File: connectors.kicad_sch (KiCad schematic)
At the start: 4 parts, among them J1 Conn_01x04_Pin, J2 Conn_01x04_Pin, J3 Conn_01x08_Pin, J4 Conn_02x03_Odd_Even

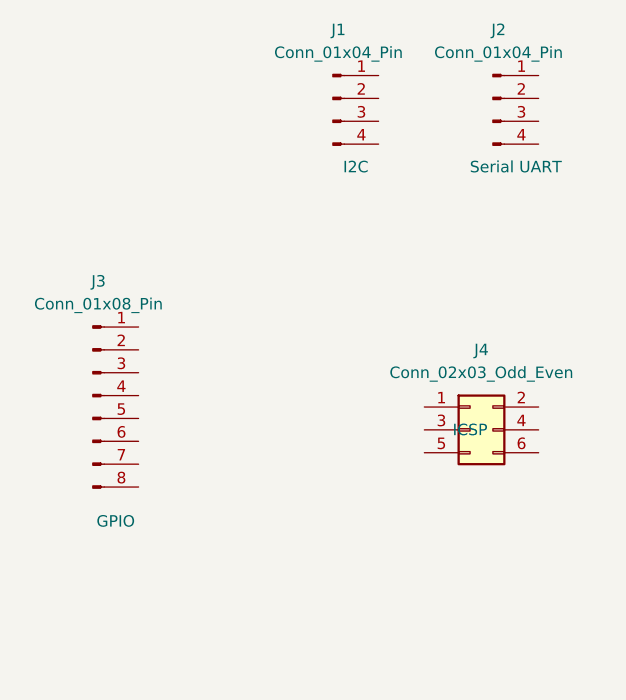
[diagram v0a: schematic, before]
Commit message: changed location of components
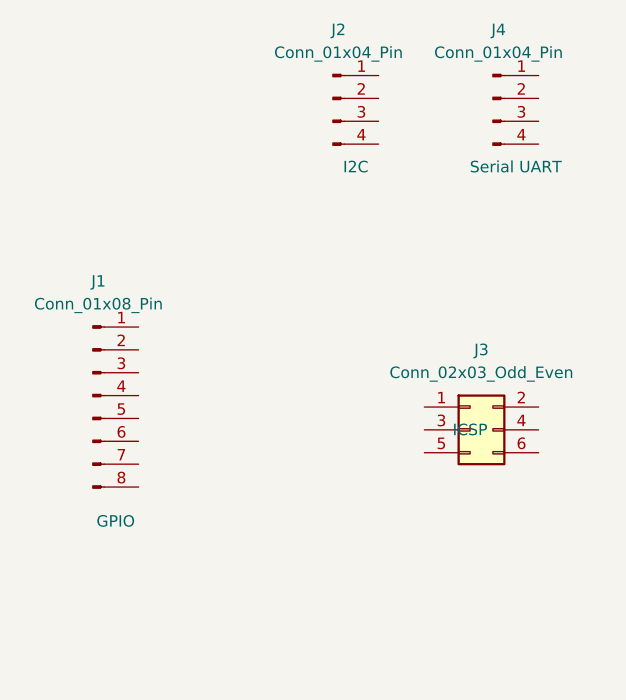
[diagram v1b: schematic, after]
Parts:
- renumbered J3 to J1, J1 to J2, J4 to J3, J2 to J4
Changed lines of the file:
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@@
 		(dnp no)
 		(fields_autoplaced yes)
-		(property "Reference" "J4"
+		(property "Reference" "J3"
 			(at 142.24 121.92 0)
 			(effects
@@
 			(project ""
 				(path "/f5eacbf3-5133-41a8-b529-b36a541e7d42/3a63fbca-d63c-4992-8461-2559cf5d4fe8"
-					(reference "J4")
+					(reference "J3")
 					(unit 1)
 				)
@@
 		(on_board yes)
 		(dnp no)
-		(property "Reference" "J1"
+		(property "Reference" "J2"
 			(at 126.365 86.36 0)
 			(effects
@@
 			(project ""
 				(path "/f5eacbf3-5133-41a8-b529-b36a541e7d42/3a63fbca-d63c-4992-8461-2559cf5d4fe8"
-					(reference "J1")
+					(reference "J2")
 					(unit 1)
 				)
@@
 		(on_board yes)
 		(dnp no)
-		(property "Reference" "J3"
+		(property "Reference" "J1"
 			(at 99.695 114.3 0)
 			(effects
@@
 			(project ""
 				(path "/f5eacbf3-5133-41a8-b529-b36a541e7d42/3a63fbca-d63c-4992-8461-2559cf5d4fe8"
-					(reference "J3")
+					(reference "J1")
 					(unit 1)
 				)
@@
 		(on_board yes)
 		(dnp no)
-		(property "Reference" "J2"
+		(property "Reference" "J4"
 			(at 144.145 86.36 0)
 			(effects
@@
 			(project "MCU Datalogger"
 				(path "/f5eacbf3-5133-41a8-b529-b36a541e7d42/3a63fbca-d63c-4992-8461-2559cf5d4fe8"
-					(reference "J2")
+					(reference "J4")
 					(unit 1)
 				)

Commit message: Added 3rd party footprints
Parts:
- removed J1: Conn_01x08_Pin, symbol Connector:Conn_01x08_Pin
- added J1: Conn_01x09_Pin, Connector_PinHeader_2.54mm:PinHeader_1x09_P2.54mm_Vertical, symbol Connector:Conn_01x09_Pin
- J2, J4: footprint (none) -> Connector_PinHeader_2.54mm:PinHeader_1x04_P2.54mm_Vertical
- J3: footprint (none) -> Connector_PinHeader_2.54mm:PinHeader_2x03_P2.54mm_Vertical
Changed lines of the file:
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@@
 			)
 		)
-		(property "Footprint" ""
+		(property "Footprint" "Connector_PinHeader_2.54mm:PinHeader_2x03_P2.54mm_Vertical"
 			(at 140.97 130.81 0)
 			(effects
@@
 			)
 		)
-		(property "Footprint" ""
+		(property "Footprint" "Connector_PinHeader_2.54mm:PinHeader_1x04_P2.54mm_Vertical"
 			(at 125.73 93.98 0)
 			(effects
@@
 	)
 	(symbol
-		(lib_id "Connector:Conn_01x08_Pin")
-		(at 99.06 127 0)
+		(lib_id "Connector:Conn_01x09_Pin")
+		(at 110.49 144.78 0)
 		(unit 1)
 		(exclude_from_sim no)
@@
 		(dnp no)
 		(property "Reference" "J1"
-			(at 99.695 114.3 0)
-			(effects
-				(font
-					(size 1.27 1.27)
-				)
-			)
-		)
-		(property "Value" "Conn_01x08_Pin"
-			(at 99.695 116.84 0)
-			(effects
-				(font
-					(size 1.27 1.27)
-				)
-			)
-		)
-		(property "Footprint" ""
-			(at 99.06 127 0)
+			(at 111.125 129.54 0)
+			(effects
+				(font
+					(size 1.27 1.27)
+				)
+			)
+		)
+		(property "Value" "Conn_01x09_Pin"
+			(at 111.125 132.08 0)
+			(effects
+				(font
+					(size 1.27 1.27)
+				)
+			)
+		)
+		(property "Footprint" "Connector_PinHeader_2.54mm:PinHeader_1x09_P2.54mm_Vertical"
+			(at 110.49 144.78 0)
 			(effects
 				(font
@@
 		)
 		(property "Datasheet" "~"
-			(at 99.06 127 0)
-			(effects
-				(font
-					(size 1.27 1.27)
-				)
-				(hide yes)
-			)
-		)
-		(property "Description" "Generic connector, single row, 01x08, script generated"
-			(at 99.06 127 0)
+			(at 110.49 144.78 0)
+			(effects
+				(font
+					(size 1.27 1.27)
+				)
+				(hide yes)
+			)
+		)
+		(property "Description" "Generic connector, single row, 01x09, script generated"
+			(at 110.49 144.78 0)
 			(effects
 				(font
@@
 		)
 		(property "Purpose" "GPIO"
-			(at 101.6 140.97 0)
-			(effects
-				(font
-					(size 1.27 1.27)
-				)
-			)
+			(at 113.03 157.48 0)
+			(effects
+				(font
+					(size 1.27 1.27)
+				)
+			)
+		)
+		(pin "3"
+		)
+		(pin "4"
 		)
 		(pin "5"
 		)
-		(pin "3"
-		)
-		(pin "4"
+		(pin "9"
+		)
+		(pin "8"
+		)
+		(pin "2"
+		)
+		(pin "6"
 		)
 		(pin "7"
 		)
-		(pin "2"
-		)
 		(pin "1"
-		)
-		(pin "6"
-		)
-		(pin "8"
 		)
 		(instances
@@
 			)
 		)
-		(property "Footprint" ""
+		(property "Footprint" "Connector_PinHeader_2.54mm:PinHeader_1x04_P2.54mm_Vertical"
 			(at 143.51 93.98 0)
 			(effects

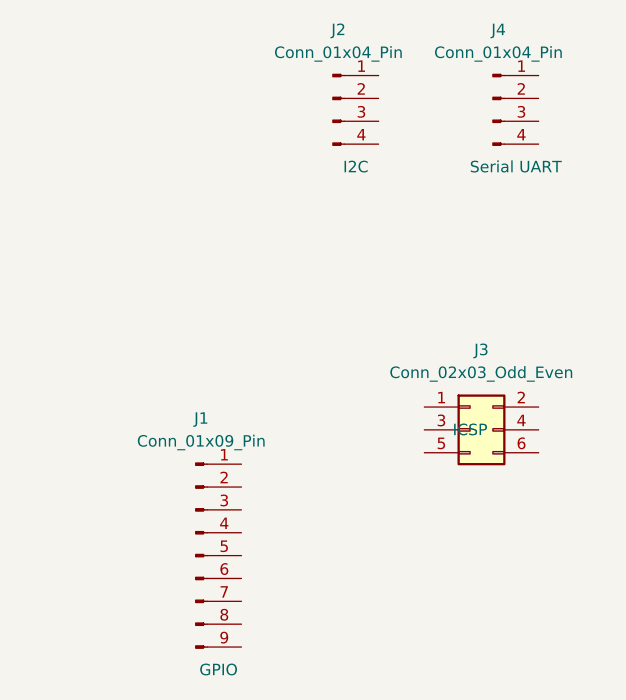
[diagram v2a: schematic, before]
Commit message: Wired connectors sheet
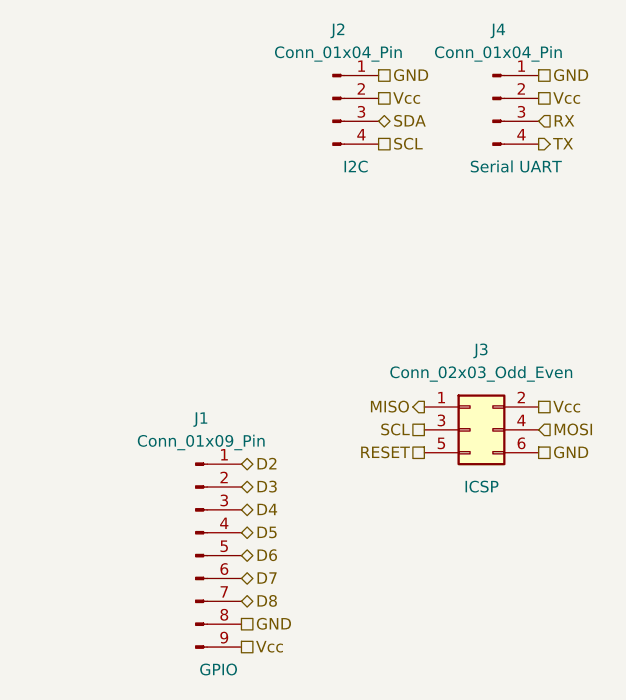
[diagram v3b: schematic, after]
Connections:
- net MISO: now reaches J3.1 (Pin_1)
- net Vcc: now reaches J3.2 (Pin_2)
- net Vcc: now also J1.9 (Pin_9), J2.2 (Pin_2), J4.2 (Pin_2)
- net SCL: now reaches J3.3 (Pin_3)
- net SCL: now also J2.4 (Pin_4)
- net MOSI: now reaches J3.4 (Pin_4)
- net RESET: now reaches J3.5 (Pin_5)
- net GND: now reaches J3.6 (Pin_6)
- net GND: now also J1.8 (Pin_8), J2.1 (Pin_1), J4.1 (Pin_1)
- net SDA: now reaches J2.3 (Pin_3)
- net D2: now reaches J1.1 (Pin_1)
- net D3: now reaches J1.2 (Pin_2)
- net D4: now reaches J1.3 (Pin_3)
- net D5: now reaches J1.4 (Pin_4)
- net D6: now reaches J1.5 (Pin_5)
- net D7: now reaches J1.6 (Pin_6)
- net D8: now reaches J1.7 (Pin_7)
- net RX: now reaches J4.3 (Pin_3)
- net TX: now reaches J4.4 (Pin_4)

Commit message: Fixed errors in the schematic
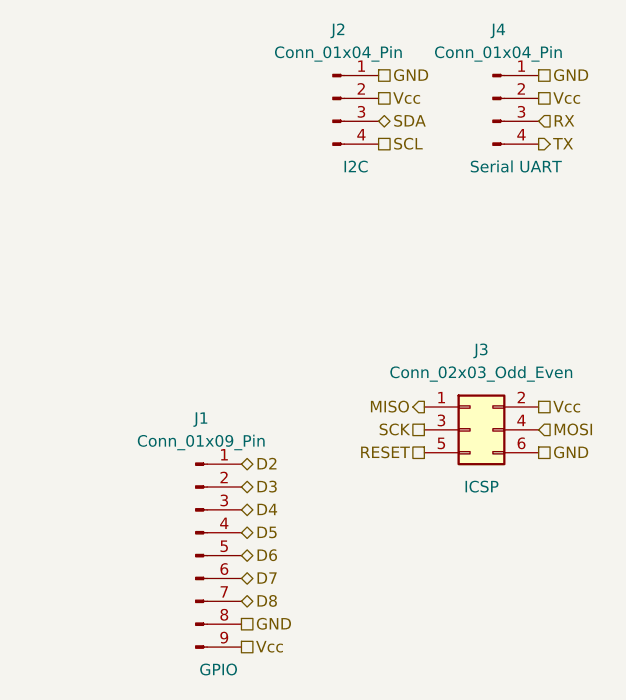
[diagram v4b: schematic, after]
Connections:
- net SCL: no longer J3.3 (Pin_3)
- new net SCK: J3.3 (Pin_3)
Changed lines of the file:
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@@
 		)
 	)
-	(hierarchical_label "SCL"
+	(hierarchical_label "SCK"
 		(shape passive)
 		(at 135.89 130.81 180)
